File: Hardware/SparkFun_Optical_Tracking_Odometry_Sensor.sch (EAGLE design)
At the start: 49 parts, among them J1 QWIIC_RIGHT_ANGLE, J2 QWIIC_RIGHT_ANGLE, Q1 100mA/20V/3.8Ω, Q2 100mA/20V/3.8Ω, U1 PAA5160E1-Q, U2 LSM6DS0, U3 STM32C011F6U6, U4 RT9080-18GJ5

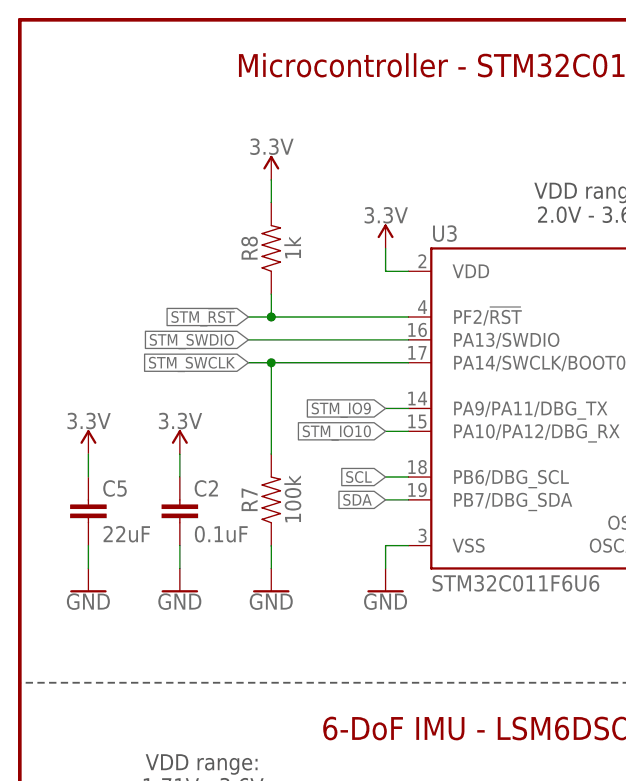
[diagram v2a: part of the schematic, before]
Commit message: Replace external reset pullup with decoupling cap
Turns out the datasheet calls for it, whoops!
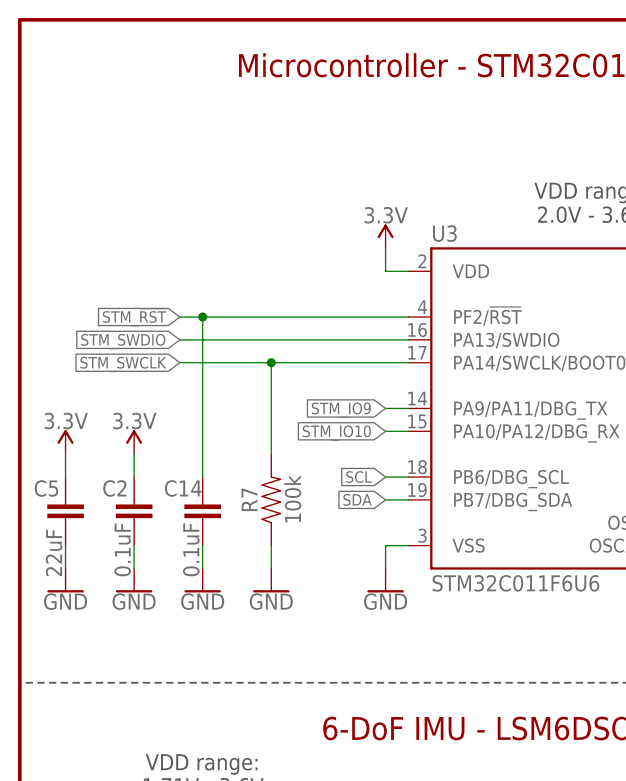
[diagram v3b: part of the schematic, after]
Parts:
- removed R8: 1k, SparkFun-Resistors:1KOHM-0603-1/10W-1%
- added C14: 0.1uF, SparkFun-Capacitors:0.1UF-0603-25V-(+80/-20%)
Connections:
- net 3.3V: no longer R8.2
- net GND: now also C14.2
- net STM_!RST!: now also C14.1; no longer R8.1
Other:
- moved on the sheet: C2, C5
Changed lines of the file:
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@@
 <part name="R7" library="SparkFun-Resistors" deviceset="100KOHM" device="-0603-1/10W-1%" value="100k"/>
 <part name="GND25" library="SparkFun-PowerSymbols" deviceset="GND" device=""/>
-<part name="R8" library="SparkFun-Resistors" deviceset="1KOHM" device="-0603-1/10W-1%" value="1k"/>
-<part name="SUPPLY26" library="SparkFun-PowerSymbols" deviceset="3.3V" device=""/>
+<part name="GND26" library="SparkFun-PowerSymbols" deviceset="GND" device=""/>
+<part name="C14" library="SparkFun-Capacitors" deviceset="0.1UF" device="-0603-25V-(+80/-20%)" value="0.1uF"/>
 </parts>
 <sheets>
@@
 <attribute name="VALUE" x="90.424" y="8.001" size="1.778" layer="96" font="vector"/>
 </instance>
-<instance part="C2" gate="G$1" x="17.78" y="129.54" smashed="yes">
-<attribute name="NAME" x="19.304" y="132.461" size="1.778" layer="95" font="vector"/>
-<attribute name="VALUE" x="19.304" y="127.381" size="1.778" layer="96" font="vector"/>
-</instance>
-<instance part="SUPPLY13" gate="G$1" x="17.78" y="137.16" smashed="yes">
-<attribute name="VALUE" x="17.78" y="139.954" size="1.778" layer="96" font="vector" align="bottom-center"/>
-</instance>
-<instance part="GND10" gate="1" x="17.78" y="121.92" smashed="yes">
-<attribute name="VALUE" x="17.78" y="121.666" size="1.778" layer="96" font="vector" align="top-center"/>
+<instance part="C2" gate="G$1" x="12.7" y="129.54" smashed="yes">
+<attribute name="NAME" x="9.144" y="132.461" size="1.778" layer="95" font="vector"/>
+<attribute name="VALUE" x="12.319" y="123.444" size="1.778" layer="96" font="vector" rot="R90"/>
+</instance>
+<instance part="SUPPLY13" gate="G$1" x="12.7" y="137.16" smashed="yes">
+<attribute name="VALUE" x="12.7" y="139.954" size="1.778" layer="96" font="vector" align="bottom-center"/>
+</instance>
+<instance part="GND10" gate="1" x="12.7" y="121.92" smashed="yes">
+<attribute name="VALUE" x="12.7" y="121.666" size="1.778" layer="96" font="vector" align="top-center"/>
 </instance>
 <instance part="C3" gate="G$1" x="25.4" y="76.2" smashed="yes">
@@
 <attribute name="VALUE" x="87.884" y="165.1" size="1.778" layer="96" font="vector" rot="R90" align="top-center"/>
 </instance>
-<instance part="C5" gate="G$1" x="7.62" y="129.54" smashed="yes">
-<attribute name="NAME" x="9.144" y="132.461" size="1.778" layer="95" font="vector"/>
-<attribute name="VALUE" x="9.144" y="127.381" size="1.778" layer="96" font="vector"/>
-</instance>
-<instance part="GND13" gate="1" x="7.62" y="121.92" smashed="yes">
-<attribute name="VALUE" x="7.62" y="121.666" size="1.778" layer="96" font="vector" align="top-center"/>
-</instance>
-<instance part="SUPPLY17" gate="G$1" x="7.62" y="137.16" smashed="yes">
-<attribute name="VALUE" x="7.62" y="139.954" size="1.778" layer="96" font="vector" align="bottom-center"/>
+<instance part="C5" gate="G$1" x="5.08" y="129.54" smashed="yes">
+<attribute name="NAME" x="1.524" y="132.461" size="1.778" layer="95" font="vector"/>
+<attribute name="VALUE" x="4.699" y="123.444" size="1.778" layer="96" font="vector" rot="R90"/>
+</instance>
+<instance part="GND13" gate="1" x="5.08" y="121.92" smashed="yes">
+<attribute name="VALUE" x="5.08" y="121.666" size="1.778" layer="96" font="vector" align="top-center"/>
+</instance>
+<instance part="SUPPLY17" gate="G$1" x="5.08" y="137.16" smashed="yes">
+<attribute name="VALUE" x="5.08" y="139.954" size="1.778" layer="96" font="vector" align="bottom-center"/>
 </instance>
 <instance part="R7" gate="G$1" x="27.94" y="132.08" smashed="yes" rot="R90">
@@
 <attribute name="VALUE" x="27.94" y="121.666" size="1.778" layer="96" font="vector" align="top-center"/>
 </instance>
-<instance part="R8" gate="G$1" x="27.94" y="160.02" smashed="yes" rot="R90">
-<attribute name="NAME" x="26.416" y="160.02" size="1.778" layer="95" font="vector" rot="R90" align="bottom-center"/>
-<attribute name="VALUE" x="29.464" y="160.02" size="1.778" layer="96" font="vector" rot="R90" align="top-center"/>
-</instance>
-<instance part="SUPPLY26" gate="G$1" x="27.94" y="167.64" smashed="yes">
-<attribute name="VALUE" x="27.94" y="170.434" size="1.778" layer="96" font="vector" align="bottom-center"/>
+<instance part="GND26" gate="1" x="20.32" y="121.92" smashed="yes">
+<attribute name="VALUE" x="20.32" y="121.666" size="1.778" layer="96" font="vector" align="top-center"/>
+</instance>
+<instance part="C14" gate="G$1" x="20.32" y="129.54" smashed="yes">
+<attribute name="NAME" x="16.002" y="132.461" size="1.778" layer="95" font="vector"/>
+<attribute name="VALUE" x="19.939" y="123.444" size="1.778" layer="96" font="vector" rot="R90"/>
 </instance>
 </instances>
@@
 <pinref part="GND10" gate="1" pin="GND"/>
 <pinref part="C2" gate="G$1" pin="2"/>
-<wire x1="17.78" y1="124.46" x2="17.78" y2="127" width="0.1524" layer="91"/>
+<wire x1="12.7" y1="124.46" x2="12.7" y2="127" width="0.1524" layer="91"/>
 </segment>
 <segment>
@@
 <pinref part="GND13" gate="1" pin="GND"/>
 <pinref part="C5" gate="G$1" pin="2"/>
-<wire x1="7.62" y1="124.46" x2="7.62" y2="127" width="0.1524" layer="91"/>
+<wire x1="5.08" y1="124.46" x2="5.08" y2="127" width="0.1524" layer="91"/>
 </segment>
 <segment>
@@
 <pinref part="GND8" gate="1" pin="GND"/>
 <wire x1="134.62" y1="78.74" x2="134.62" y2="76.2" width="0.1524" layer="91"/>
+</segment>
+<segment>
+<pinref part="GND26" gate="1" pin="GND"/>
+<wire x1="20.32" y1="124.46" x2="20.32" y2="127" width="0.1524" layer="91"/>
+<pinref part="C14" gate="G$1" pin="2"/>
 </segment>
 </net>
@@
 <pinref part="SUPPLY13" gate="G$1" pin="3.3V"/>
 <pinref part="C2" gate="G$1" pin="1"/>
-<wire x1="17.78" y1="137.16" x2="17.78" y2="134.62" width="0.1524" layer="91"/>
+<wire x1="12.7" y1="137.16" x2="12.7" y2="134.62" width="0.1524" layer="91"/>
 </segment>
 <segment>
@@
 <pinref part="SUPPLY17" gate="G$1" pin="3.3V"/>
 <pinref part="C5" gate="G$1" pin="1"/>
-<wire x1="7.62" y1="137.16" x2="7.62" y2="134.62" width="0.1524" layer="91"/>
-</segment>
-<segment>
-<pinref part="R8" gate="G$1" pin="2"/>
-<pinref part="SUPPLY26" gate="G$1" pin="3.3V"/>
-<wire x1="27.94" y1="165.1" x2="27.94" y2="167.64" width="0.1524" layer="91"/>
+<wire x1="5.08" y1="137.16" x2="5.08" y2="134.62" width="0.1524" layer="91"/>
 </segment>
 <segment>
@@
 <segment>
 <pinref part="U3" gate="G$1" pin="PF2/!RST!"/>
-<wire x1="43.18" y1="152.4" x2="27.94" y2="152.4" width="0.1524" layer="91"/>
-<label x="25.4" y="152.4" size="1.27" layer="95" font="vector" rot="R180" xref="yes"/>
-<pinref part="R8" gate="G$1" pin="1"/>
-<wire x1="27.94" y1="152.4" x2="25.4" y2="152.4" width="0.1524" layer="91"/>
-<wire x1="27.94" y1="154.94" x2="27.94" y2="152.4" width="0.1524" layer="91"/>
-<junction x="27.94" y="152.4"/>
+<wire x1="43.18" y1="152.4" x2="20.32" y2="152.4" width="0.1524" layer="91"/>
+<label x="17.78" y="152.4" size="1.27" layer="95" font="vector" rot="R180" xref="yes"/>
+<wire x1="20.32" y1="152.4" x2="17.78" y2="152.4" width="0.1524" layer="91"/>
+<wire x1="20.32" y1="134.62" x2="20.32" y2="152.4" width="0.1524" layer="91"/>
+<junction x="20.32" y="152.4"/>
+<pinref part="C14" gate="G$1" pin="1"/>
 </segment>
 <segment>
@@
 <segment>
 <pinref part="U3" gate="G$1" pin="PA13/SWDIO"/>
-<wire x1="43.18" y1="149.86" x2="25.4" y2="149.86" width="0.1524" layer="91"/>
-<label x="25.4" y="149.86" size="1.27" layer="95" font="vector" rot="R180" xref="yes"/>
+<wire x1="43.18" y1="149.86" x2="17.78" y2="149.86" width="0.1524" layer="91"/>
+<label x="17.78" y="149.86" size="1.27" layer="95" font="vector" rot="R180" xref="yes"/>
 </segment>
 <segment>
@@
 <pinref part="U3" gate="G$1" pin="PA14/SWCLK/BOOT0"/>
 <wire x1="43.18" y1="147.32" x2="27.94" y2="147.32" width="0.1524" layer="91"/>
-<label x="25.4" y="147.32" size="1.27" layer="95" font="vector" rot="R180" xref="yes"/>
+<label x="17.78" y="147.32" size="1.27" layer="95" font="vector" rot="R180" xref="yes"/>
 <pinref part="R7" gate="G$1" pin="2"/>
-<wire x1="27.94" y1="147.32" x2="25.4" y2="147.32" width="0.1524" layer="91"/>
+<wire x1="27.94" y1="147.32" x2="17.78" y2="147.32" width="0.1524" layer="91"/>
 <wire x1="27.94" y1="137.16" x2="27.94" y2="147.32" width="0.1524" layer="91"/>
 <junction x="27.94" y="147.32"/>
